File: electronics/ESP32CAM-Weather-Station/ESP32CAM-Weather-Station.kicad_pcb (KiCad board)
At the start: 4 copper layers, 100 x 100 mm, 0 parts

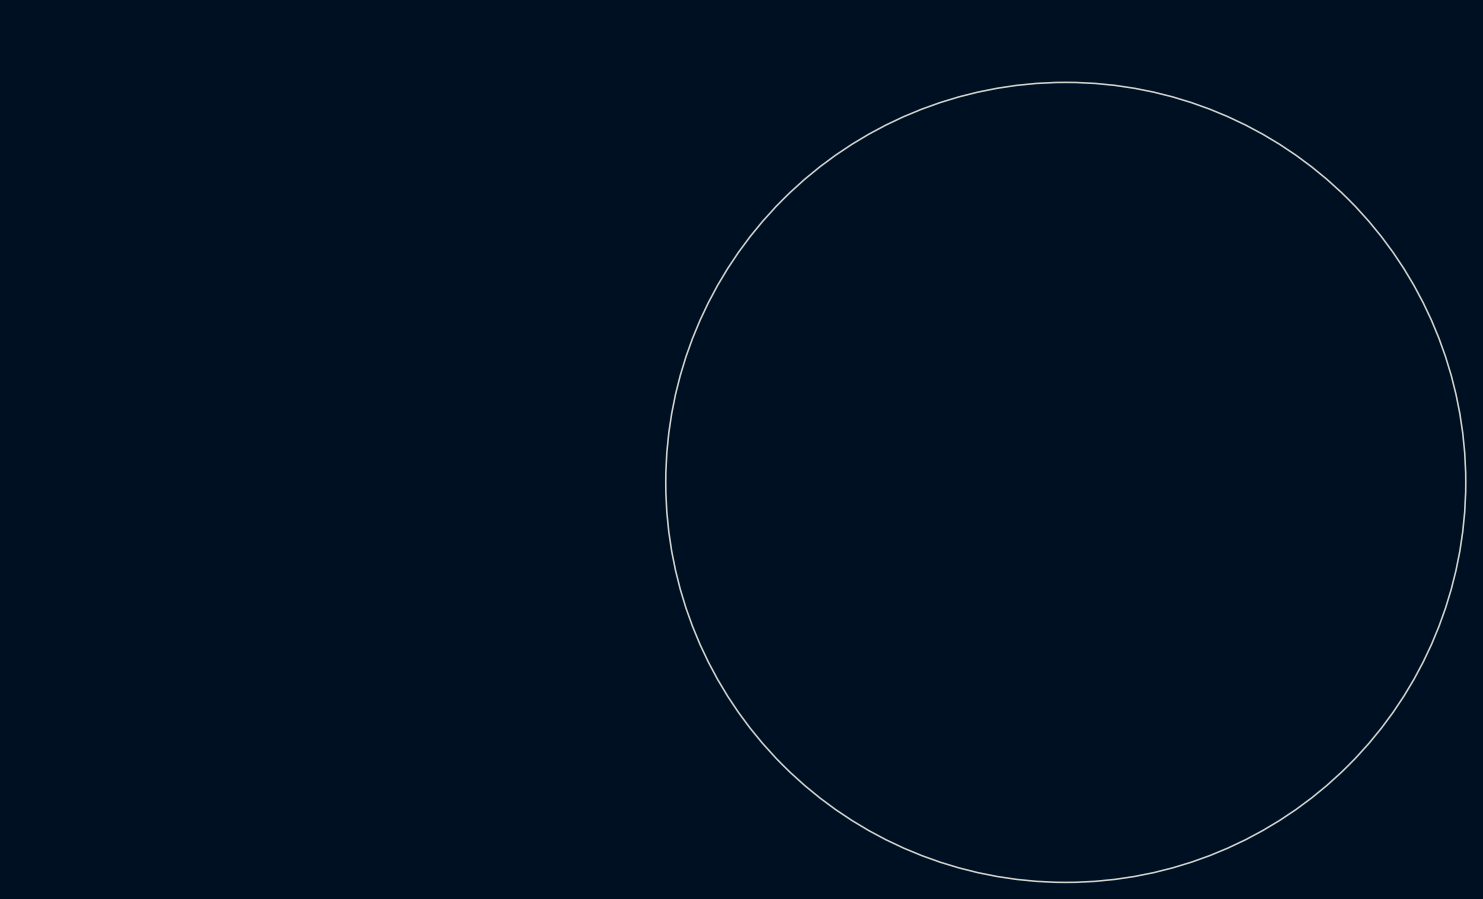
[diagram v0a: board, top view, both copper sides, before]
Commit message: [WIP] Placed Basic Connectors.
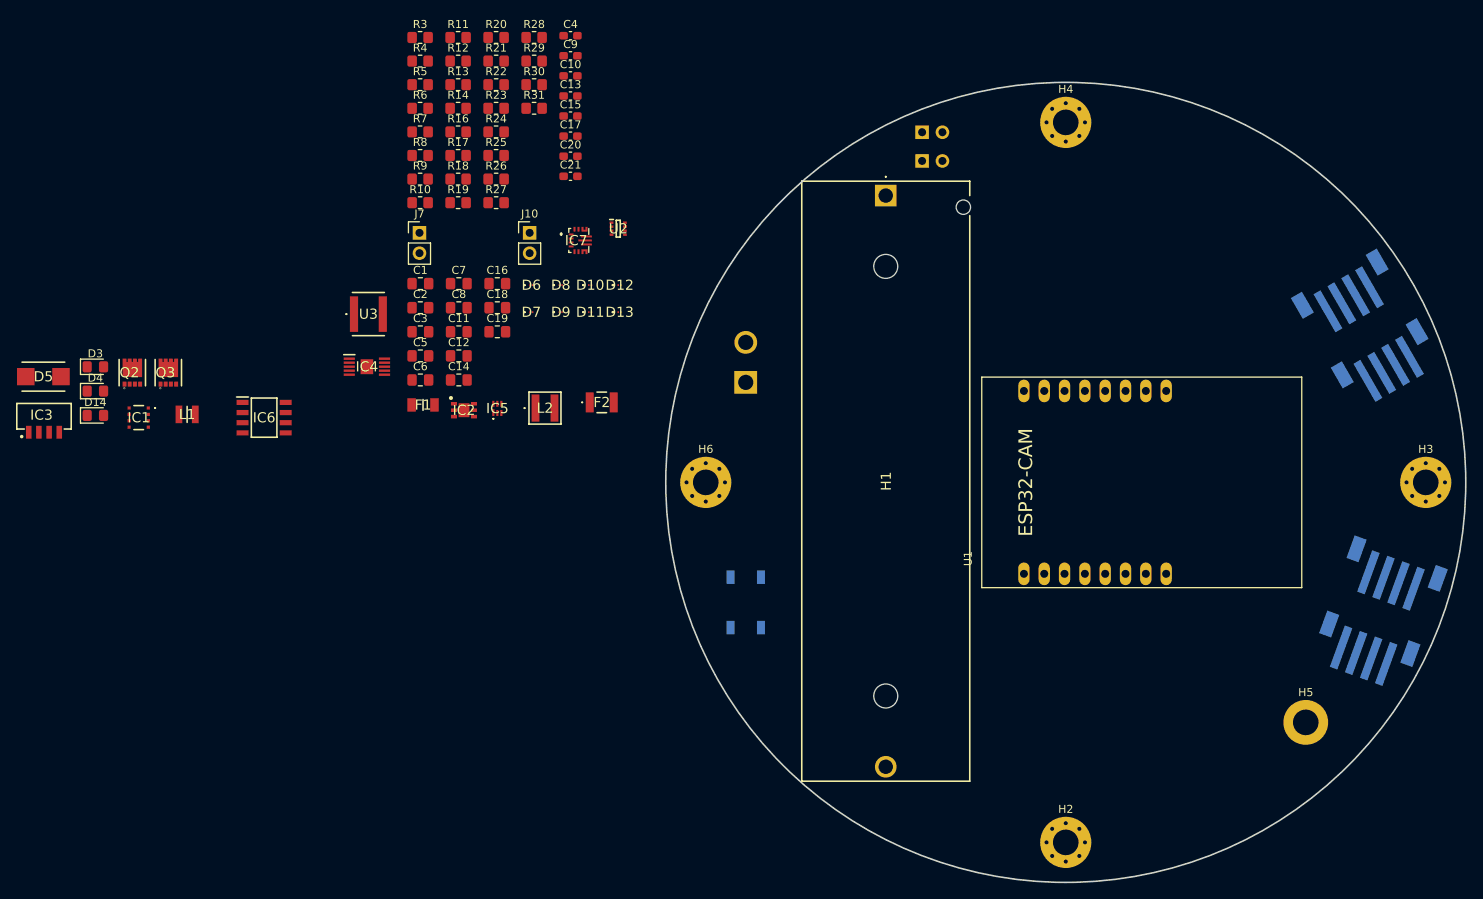
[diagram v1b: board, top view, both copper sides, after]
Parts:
- added C1: 0.1uF, Capacitor_SMD:C_0805_2012Metric_Pad1.18x1.45mm_HandSolder, F.Cu at (69.3, 75.2)
- added C10: 10uF, Capacitor_SMD:C_0603_1608Metric_Pad1.08x0.95mm_HandSolder, F.Cu at (88.1, 49.2)
- added C11: 10uF, Capacitor_SMD:C_0805_2012Metric_Pad1.18x1.45mm_HandSolder, F.Cu at (74.1, 81.2)
- added C12: 10uF, Capacitor_SMD:C_0805_2012Metric_Pad1.18x1.45mm_HandSolder, F.Cu at (74.1, 84.2)
- added C13: 100nF, Capacitor_SMD:C_0603_1608Metric_Pad1.08x0.95mm_HandSolder, F.Cu at (88.1, 51.7)
- added C14: 10uF, Capacitor_SMD:C_0805_2012Metric_Pad1.18x1.45mm_HandSolder, F.Cu at (74.1, 87.2)
- added C15: 100nF, Capacitor_SMD:C_0603_1608Metric_Pad1.08x0.95mm_HandSolder, F.Cu at (88.1, 54.2)
- added C16: 10uF, Capacitor_SMD:C_0805_2012Metric_Pad1.18x1.45mm_HandSolder, F.Cu at (78.9, 75.2)
- added C17: 100nF, Capacitor_SMD:C_0603_1608Metric_Pad1.08x0.95mm_HandSolder, F.Cu at (88.1, 56.7)
- added C18: 1uF, Capacitor_SMD:C_0805_2012Metric_Pad1.18x1.45mm_HandSolder, F.Cu at (78.9, 78.2)
- added C19: 1uF, Capacitor_SMD:C_0805_2012Metric_Pad1.18x1.45mm_HandSolder, F.Cu at (78.9, 81.2)
- added C2: 1uF, Capacitor_SMD:C_0805_2012Metric_Pad1.18x1.45mm_HandSolder, F.Cu at (69.3, 78.2)
- added C20: 100nF, Capacitor_SMD:C_0603_1608Metric_Pad1.08x0.95mm_HandSolder, F.Cu at (88.1, 59.2)
- added C21: 100nF, Capacitor_SMD:C_0603_1608Metric_Pad1.08x0.95mm_HandSolder, F.Cu at (88.1, 61.7)
- added C3: 1uF, Capacitor_SMD:C_0805_2012Metric_Pad1.18x1.45mm_HandSolder, F.Cu at (69.3, 81.2)
- added C4: 22uF, Capacitor_SMD:C_0603_1608Metric_Pad1.08x0.95mm_HandSolder, F.Cu at (88.1, 44.2)
- added C5: 47uF, Capacitor_SMD:C_0805_2012Metric_Pad1.18x1.45mm_HandSolder, F.Cu at (69.3, 84.2)
- added C6: 22uF, Capacitor_SMD:C_0805_2012Metric_Pad1.18x1.45mm_HandSolder, F.Cu at (69.3, 87.2)
- added C7: 22uF, Capacitor_SMD:C_0805_2012Metric_Pad1.18x1.45mm_HandSolder, F.Cu at (74.1, 75.2)
- added C8: 22uF, Capacitor_SMD:C_0805_2012Metric_Pad1.18x1.45mm_HandSolder, F.Cu at (74.1, 78.2)
- added C9: 10uF, Capacitor_SMD:C_0603_1608Metric_Pad1.08x0.95mm_HandSolder, F.Cu at (88.1, 46.7)
- added D10: ESDZV5H-1BU2, ESDZV5H-1BU2:ESDZV5H1BU2, F.Cu at (90.5, 75.3)
- added D11: ESDZV5H-1BU2, ESDZV5H-1BU2:ESDZV5H1BU2, F.Cu at (90.5, 78.7)
- added D12: ESDZV5H-1BU2, ESDZV5H-1BU2:ESDZV5H1BU2, F.Cu at (94.2, 75.3)
- added D13: ESDZV5H-1BU2, ESDZV5H-1BU2:ESDZV5H1BU2, F.Cu at (94.2, 78.7)
- added D14: LED_RED, LED_SMD:LED_0805_2012Metric_Pad1.15x1.40mm_HandSolder, F.Cu at (28.7, 91.6)
- added D3: LED_RED, LED_SMD:LED_0805_2012Metric_Pad1.15x1.40mm_HandSolder, F.Cu at (28.7, 85.6)
- added D4: LED_RED, LED_SMD:LED_0805_2012Metric_Pad1.15x1.40mm_HandSolder, F.Cu at (28.7, 88.6)
- added D5: SMBJ20CA-TR, SMBJ20CA-TR:DIONM5436X265N, F.Cu at (22.2, 86.8)
- added D6: ESDZV5H-1BU2, ESDZV5H-1BU2:ESDZV5H1BU2, F.Cu at (83.2, 75.3)
- added D7: ESDZV5H-1BU2, ESDZV5H-1BU2:ESDZV5H1BU2, F.Cu at (83.2, 78.7)
- added D8: ESDZV5H-1BU2, ESDZV5H-1BU2:ESDZV5H1BU2, F.Cu at (86.9, 75.3)
- added D9: ESDZV5H-1BU2, ESDZV5H-1BU2:ESDZV5H1BU2, F.Cu at (86.9, 78.7)
- added F1: SF-1206FP400-2, SF-1206FP400-2:FUSC3116X70N, F.Cu at (69.7, 90.3)
- added F2: MF-USHT125KX_12-2, MF-USHT125KX_12-2:MFUSHT125KX122, F.Cu at (92.0, 90.0)
- added H1: 12BHC186P2-GR, 12BHC186P2-GR:12BHC186P2GR, F.Cu at (127.5, 64.2)
- added H2: MountingHole, MountingHole:MountingHole_3.2mm_M3_Pad_Via, F.Cu at (150.0, 145.0)
- added H3: MountingHole, MountingHole:MountingHole_3.2mm_M3_Pad_Via, F.Cu at (195.0, 100.0)
- added H4: MountingHole, MountingHole:MountingHole_3.2mm_M3_Pad_Via, F.Cu at (150.0, 55.0)
- added H5: MountingHole_Pad, MountingHole:MountingHole_3.2mm_M3_DIN965_Pad, F.Cu at (180.0, 130.0)
- added H6: MountingHole, MountingHole:MountingHole_3.2mm_M3_Pad_Via, F.Cu at (105.0, 100.0)
- added IC1: BME688, BME688:BME688, F.Cu at (34.1, 91.9)
- added IC2: SGP41-D-R4, SGP41-D-R4:SON80P244X244X95-7N, F.Cu at (74.8, 91.0)
- added IC3: VEML7700-TT, VEML7700-TT:VEML7700, F.Cu at (18.9, 93.3)
- added IC4: BQ24093DGQR, BQ24093DGQR:SOP50P490X110-11N, F.Cu at (62.6, 85.5)
- added IC5: BQ29707DSET, BQ29707DSET:TPS610985DSET, F.Cu at (79.0, 90.8)
- added IC6: MCP3426A0T-E_SN, MCP3426A0T-E_SN:SOIC127P600X175-8N, F.Cu at (49.8, 91.9)
- added IC7: TPS63070RNMR, TPS63070RNMR:TPS630701RNMR, F.Cu at (88.6, 69.8)
- added J1: B4B-PH-SM4-TB_LF__SN_, B4B-PH-SM4-TB_LF__SN_:B4B-PH-SM4_1, B.Cu at (192.3, 107.8)
- added J10: Conn_01x02_Pin, Connector_PinHeader_2.54mm:PinHeader_1x02_P2.54mm_Vertical, F.Cu at (83.0, 68.8)
- added J2: B4B-PH-SM4-TB_LF__SN_, B4B-PH-SM4-TB_LF__SN_:B4B-PH-SM4_1, B.Cu at (188.9, 117.2)
- added J3: B4B-PH-SM4-TB_LF__SN_, B4B-PH-SM4-TB_LF__SN_:B4B-PH-SM4_1, B.Cu at (183.0, 73.0)
- added J4: B4B-PH-SM4-TB_LF__SN_, B4B-PH-SM4-TB_LF__SN_:B4B-PH-SM4_1, B.Cu at (188.0, 81.7)
- added J6: XT30UPB-M, XT30UPB-M:AMASS_XT30UPB-M, B.Cu at (110.0, 85.0)
- added J7: Conn_01x02_Pin, Connector_PinHeader_2.54mm:PinHeader_1x02_P2.54mm_Vertical, F.Cu at (69.2, 68.8)
- added J8: Conn_01x02_Pin, Connector_PinHeader_2.54mm:PinHeader_1x02_P2.54mm_Vertical, B.Cu at (132.0, 56.2)
- added J9: Conn_01x02_Pin, Connector_PinHeader_2.54mm:PinHeader_1x02_P2.54mm_Vertical, B.Cu at (132.0, 59.8)
- added L1: DFE252012P-1R0M=P2, DFE252012P-1R0M=P2:DFE2HCAH1R0MJ0L, F.Cu at (40.2, 91.5)
- added L2: XFL4020-152MEC, XFL4020-152MEC:XFL4020152MEC, F.Cu at (84.9, 90.7)
- added Q2: CSD16406Q3, CSD16406Q3:DQG_VSON-CLIP, F.Cu at (33.3, 86.3)
- added Q3: CSD16406Q3, CSD16406Q3:DQG_VSON-CLIP, F.Cu at (37.8, 86.3)
- added R10: 1k, Resistor_SMD:R_0805_2012Metric_Pad1.20x1.40mm_HandSolder, F.Cu at (69.3, 65.0)
- added R11: 1k, Resistor_SMD:R_0805_2012Metric_Pad1.20x1.40mm_HandSolder, F.Cu at (74.0, 44.4)
- added R12: 1k, Resistor_SMD:R_0805_2012Metric_Pad1.20x1.40mm_HandSolder, F.Cu at (74.0, 47.3)
- added R13: 1k, Resistor_SMD:R_0805_2012Metric_Pad1.20x1.40mm_HandSolder, F.Cu at (74.0, 50.3)
- added R14: 1k, Resistor_SMD:R_0805_2012Metric_Pad1.20x1.40mm_HandSolder, F.Cu at (74.0, 53.2)
- added R16: 330, Resistor_SMD:R_0805_2012Metric_Pad1.20x1.40mm_HandSolder, F.Cu at (74.0, 56.2)
- added R17: 2.2k, Resistor_SMD:R_0805_2012Metric_Pad1.20x1.40mm_HandSolder, F.Cu at (74.0, 59.1)
- added R18: 1k, Resistor_SMD:R_0805_2012Metric_Pad1.20x1.40mm_HandSolder, F.Cu at (74.0, 62.1)
- added R19: 1k, Resistor_SMD:R_0805_2012Metric_Pad1.20x1.40mm_HandSolder, F.Cu at (74.0, 65.0)
- added R20: 549, Resistor_SMD:R_0805_2012Metric_Pad1.20x1.40mm_HandSolder, F.Cu at (78.8, 44.4)
- added R21: 10k, Resistor_SMD:R_0805_2012Metric_Pad1.20x1.40mm_HandSolder, F.Cu at (78.8, 47.3)
- added R22: 1k, Resistor_SMD:R_0805_2012Metric_Pad1.20x1.40mm_HandSolder, F.Cu at (78.8, 50.3)
- added R23: 91k, Resistor_SMD:R_0805_2012Metric_Pad1.20x1.40mm_HandSolder, F.Cu at (78.8, 53.2)
- added R24: 511k, Resistor_SMD:R_0805_2012Metric_Pad1.20x1.40mm_HandSolder, F.Cu at (78.8, 56.2)
- added R25: 10k, Resistor_SMD:R_0805_2012Metric_Pad1.20x1.40mm_HandSolder, F.Cu at (78.8, 59.1)
- added R26: 10k, Resistor_SMD:R_0805_2012Metric_Pad1.20x1.40mm_HandSolder, F.Cu at (78.8, 62.1)
- added R27: 1k, Resistor_SMD:R_0805_2012Metric_Pad1.20x1.40mm_HandSolder, F.Cu at (78.8, 65.0)
- added R28: 680k, Resistor_SMD:R_0805_2012Metric_Pad1.20x1.40mm_HandSolder, F.Cu at (83.5, 44.4)
- added R29: 130k, Resistor_SMD:R_0805_2012Metric_Pad1.20x1.40mm_HandSolder, F.Cu at (83.5, 47.3)
- added R3: 20k, Resistor_SMD:R_0805_2012Metric_Pad1.20x1.40mm_HandSolder, F.Cu at (69.3, 44.4)
- added R30: 10, Resistor_SMD:R_0805_2012Metric_Pad1.20x1.40mm_HandSolder, F.Cu at (83.5, 50.3)
- added R31: 4.7, Resistor_SMD:R_0805_2012Metric_Pad1.20x1.40mm_HandSolder, F.Cu at (83.5, 53.2)
- added R4: 20k, Resistor_SMD:R_0805_2012Metric_Pad1.20x1.40mm_HandSolder, F.Cu at (69.3, 47.3)
- added R5: 100k, Resistor_SMD:R_0805_2012Metric_Pad1.20x1.40mm_HandSolder, F.Cu at (69.3, 50.3)
- added R6: 10k, Resistor_SMD:R_0805_2012Metric_Pad1.20x1.40mm_HandSolder, F.Cu at (69.3, 53.2)
- added R7: 10k, Resistor_SMD:R_0805_2012Metric_Pad1.20x1.40mm_HandSolder, F.Cu at (69.3, 56.2)
- added R8: 10k, Resistor_SMD:R_0805_2012Metric_Pad1.20x1.40mm_HandSolder, F.Cu at (69.3, 59.1)
- added R9: 1k, Resistor_SMD:R_0805_2012Metric_Pad1.20x1.40mm_HandSolder, F.Cu at (69.3, 62.1)
- added S1: TS18-5-25-SL-260-SMT-TR, TS18-5-25-SL-260-SMT-TR:TS18525SL260SMTTR, B.Cu at (110.0, 115.0)
- added U1: ESP32-CAM, ESP32-CAM:ESP32-CAM, F.Cu at (154.9, 100.0)
- added U2: TPS631000DRLR, TPS631000DRLR:SOTFL50P160X60-8N, F.Cu at (94.1, 68.3)
- added U3: GDT25-07-S1-RP, GDT25-07-S1-RP:GDT2507S1RP, F.Cu at (62.8, 79.0)
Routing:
- added copper zone on In1.Cu, net +3.3V
- added copper zone on In1.Cu, net +VBAT
- added copper zone on In2.Cu, net GND

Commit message: [WIP] Placed main battery protection components.
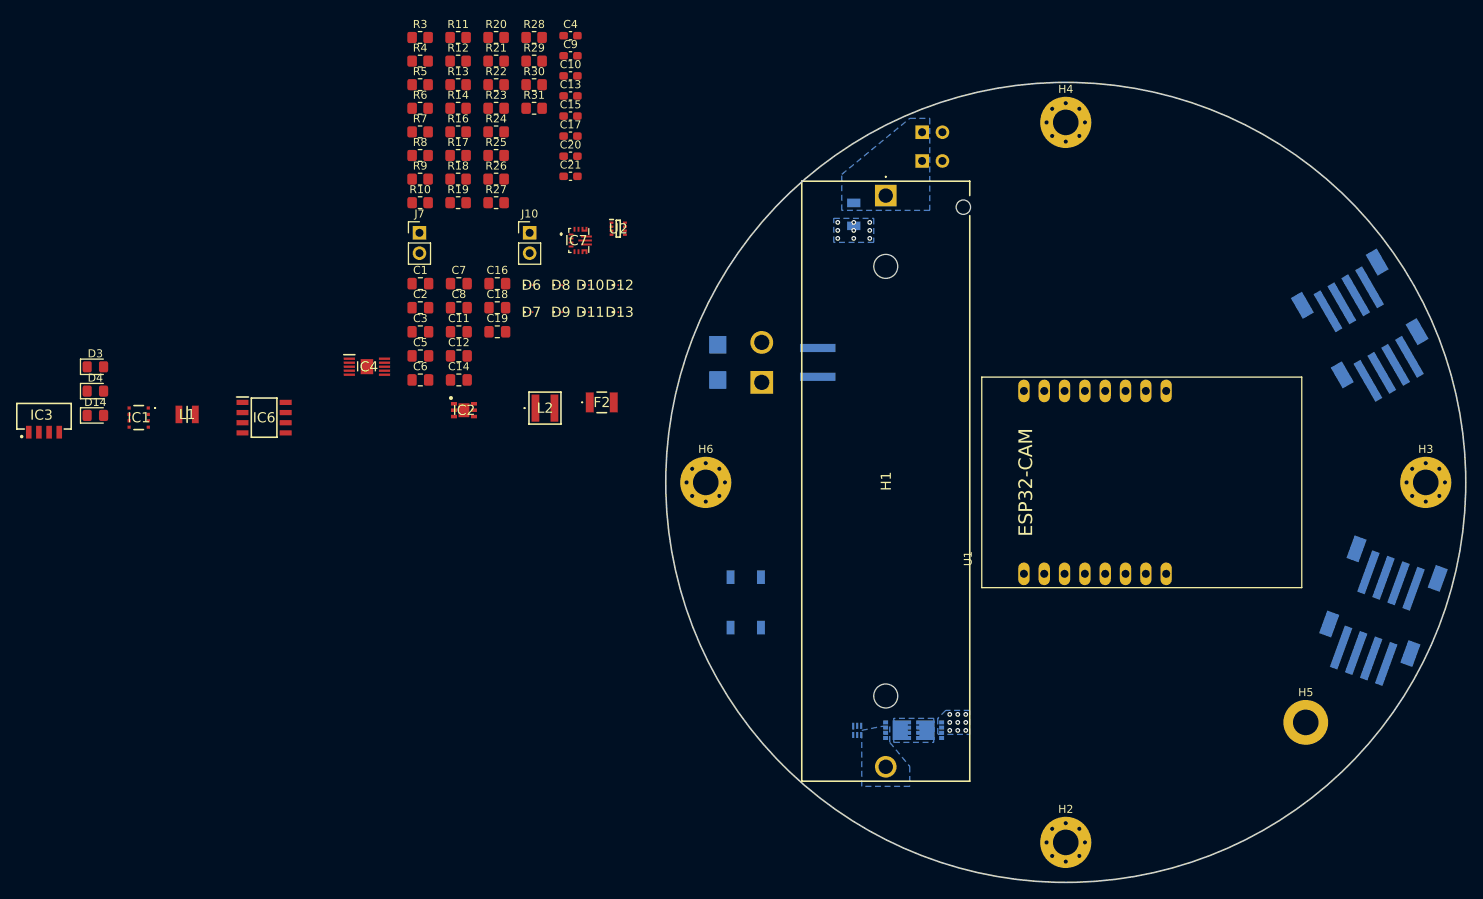
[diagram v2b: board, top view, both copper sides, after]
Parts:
- D5, F1, IC5, Q2, Q3, U3: moved to B.Cu
- moved Q2 109.3 mm to (133.0, 131.0), turned to -90 degrees
- moved Q3 101.5 mm to (128.9, 131.0), turned to 90 degrees
- moved D5 84.3 mm to (106.5, 85.0), turned to 90 degrees
- moved IC5 60.4 mm to (123.9, 131.0)
- moved F1 58.9 mm to (123.5, 66.5), turned to -90 degrees
- moved U3 56.5 mm to (119.0, 85.0), turned to 90 degrees
- moved J6 2.00 mm to (112.0, 85.0)
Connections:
- Q2 pad 9: (no net) -> Net-(Q2-D_1)
- Q3 pad 9: (no net) -> Net-(Q2-D_1)
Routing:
- net GND: vias 0 -> 9
- net +VBAT: vias 0 -> 9
- added copper zone on B.Cu, net +VBAT
- added copper zone on B.Cu, net +VBAT_UNFUSED
- added copper zone on B.Cu, net -VBAT
- added copper zone on B.Cu, net GND
- added copper zone on B.Cu, net Net-(Q2-D_1)

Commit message: [WIP] Placed basic 3v3 regulator parts.
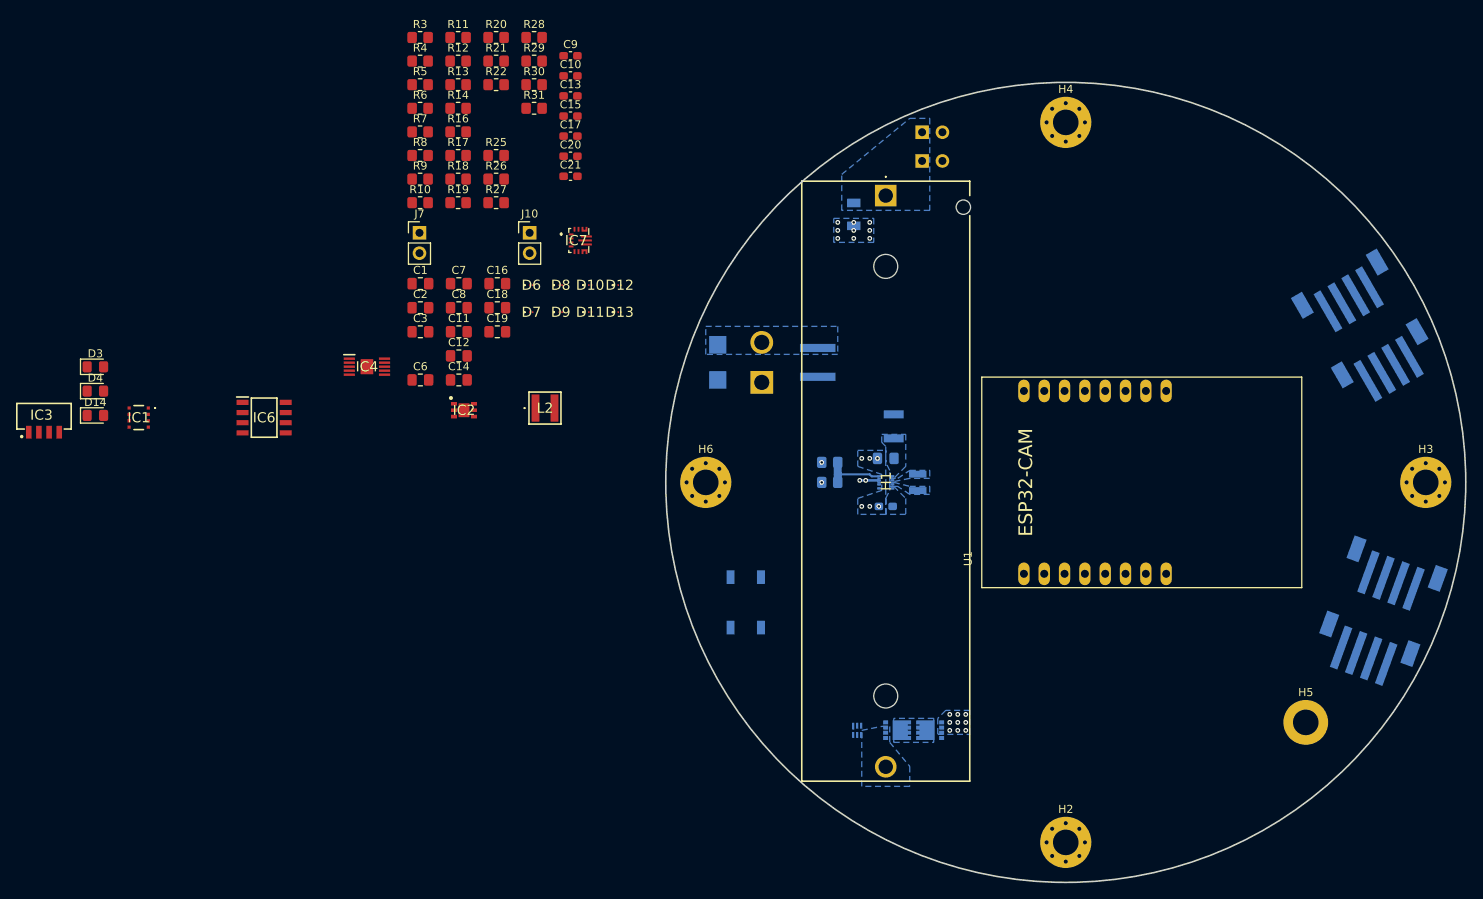
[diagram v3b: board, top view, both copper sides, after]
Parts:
- C4, C5, F2, L1, R23, R24, U2: moved to B.Cu
- moved L1 91.7 mm to (131.5, 100.0), turned to 90 degrees
- moved C4 70.8 mm to (127.5, 103.0), turned to 180 degrees
- moved R23 62.7 mm to (120.5, 100.0), turned to 180 degrees
- moved C5 59.6 mm to (127.5, 97.0), turned to 180 degrees
- moved R24 58.7 mm to (120.5, 97.5)
- moved U2 46.1 mm to (127.5, 100.0), turned to 180 degrees
- moved F2 36.6 mm to (128.5, 93.0), turned to -90 degrees
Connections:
- C5 pad 1: +3.3V -> /3V3_PREFUSE
- F2 pad 2: Net-(U2-VOUT) -> /3V3_PREFUSE
- S1 pad 1: +VBAT -> /REG_EN
- U2 pad 1: Net-(U2-VOUT) -> /3V3_PREFUSE
- U2 pad 5: +VBAT -> /REG_EN
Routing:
- net /REG_FB: track 0.00 -> 7.77 mm
- net GND: track 0.00 -> 2.41 mm, vias 9 -> 18
- net +3.3V: vias 0 -> 1
- added copper zone on B.Cu, net /3V3_PREFUSE
- added copper zone on B.Cu, net /REG_LX1
- added copper zone on B.Cu, net /REG_LX2
